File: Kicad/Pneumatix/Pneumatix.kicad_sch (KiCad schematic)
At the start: 16 parts, among them J1 705430004, J2 142-0701-801, J3 Conn_01x04_Socket, U1 E22-400T33S

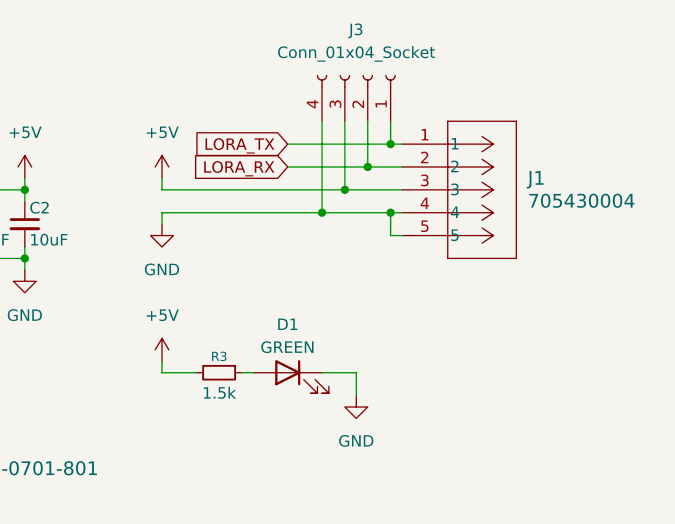
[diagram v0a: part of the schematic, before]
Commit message: wip: pcb and conception notes, fix: change molex 5 pins to 4 pins
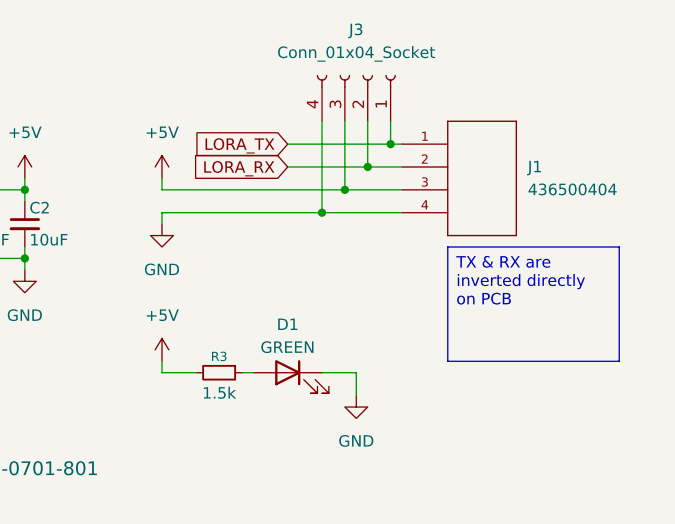
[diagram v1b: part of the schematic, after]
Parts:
- removed J1: 705430004, Pneumatix_Lib:CONN_SDA-70543-xxxx_05_MOL, symbol Pneumatix_Lib:705430004
- added J1: 436500404, Pneumatix_Lib:CONN_SD-43650-002_04_MOL, symbol Pneumatix_Lib:436500404
- H1, H2, H3: footprint MountingHole:MountingHole_2.2mm_M2 -> MountingHole:MountingHole_3.2mm_M3
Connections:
- net +5V: now also J1.3
- net GND: now also J1.4
- net LORA_RX: now also J1.2
- net LORA_TX: now also J1.1
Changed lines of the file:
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@@
 	(generator_version "10.0")
 	(paper "A4")
+	(text_box "TX & RX are inverted directly on PCB"
+		(exclude_from_sim no)
+		(at 213.36 85.09 0)
+		(size 19.05 12.7)
+		(margins 0.9525 0.9525 0.9525 0.9525)
+		(stroke
+			(width 0)
+			(type solid)
+		)
+		(fill
+			(type none)
+		)
+		(effects
+			(font
+				(size 1.27 1.27)
+			)
+			(justify left top)
+		)
+	)
 	(junction
 		(at 199.39 81.28)
@@
 	)
 	(junction
-		(at 207.01 81.28)
-		(diameter 0)
-		(color 0 0 0 0)
-	)
-	(junction
 		(at 204.47 76.2)
 		(diameter 0)
@@
 	(wire
 		(pts
-			(xy 208.28 83.82) (xy 207.01 83.82)
-		)
-		(stroke
-			(width 0)
-			(type default)
-		)
-	)
-	(wire
-		(pts
 			(xy 158.75 93.98) (xy 157.48 93.98)
 		)
@@
 	(wire
 		(pts
-			(xy 207.01 81.28) (xy 208.28 81.28)
+			(xy 181.61 81.28) (xy 208.28 81.28)
 		)
 		(stroke
@@
 	(wire
 		(pts
-			(xy 181.61 81.28) (xy 207.01 81.28)
-		)
-		(stroke
-			(width 0)
-			(type default)
-		)
-	)
-	(wire
-		(pts
 			(xy 181.61 82.55) (xy 181.61 81.28)
 		)
@@
 		(pts
 			(xy 181.61 78.74) (xy 181.61 77.47)
-		)
-		(stroke
-			(width 0)
-			(type default)
-		)
-	)
-	(wire
-		(pts
-			(xy 207.01 81.28) (xy 207.01 83.82)
 		)
 		(stroke
@@
 			)
 		)
-		(property "Footprint" "MountingHole:MountingHole_2.2mm_M2"
+		(property "Footprint" "MountingHole:MountingHole_3.2mm_M3"
 			(at 184.15 128.27 0)
 			(hide yes)
@@
 	)
 	(symbol
-		(lib_id "Pneumatix_Lib:705430004")
-		(at 208.28 73.66 0)
-		(unit 1)
-		(body_style 1)
-		(exclude_from_sim no)
-		(in_bom yes)
-		(on_board yes)
-		(in_pos_files yes)
-		(dnp no)
-		(fields_autoplaced yes)
-		(property "Reference" "J1"
-			(at 222.25 77.4699 0)
-			(show_name no)
-			(do_not_autoplace no)
-			(effects
-				(font
-					(size 1.524 1.524)
-				)
-				(justify left)
-			)
-		)
-		(property "Value" "705430004"
-			(at 222.25 80.0099 0)
-			(show_name no)
-			(do_not_autoplace no)
-			(effects
-				(font
-					(size 1.524 1.524)
-				)
-				(justify left)
-			)
-		)
-		(property "Footprint" "Pneumatix_Lib:CONN_SDA-70543-xxxx_05_MOL"
-			(at 208.28 73.66 0)
-			(hide yes)
-			(show_name no)
-			(do_not_autoplace no)
-			(effects
-				(font
-					(size 1.27 1.27)
-					(italic yes)
-				)
-			)
-		)
-		(property "Datasheet" "705430004"
-			(at 208.28 73.66 0)
-			(hide yes)
-			(show_name no)
-			(do_not_autoplace no)
-			(effects
-				(font
-					(size 1.27 1.27)
-					(italic yes)
-				)
-			)
-		)
-		(property "Description" ""
-			(at 208.28 73.66 0)
-			(hide yes)
-			(show_name no)
-			(do_not_autoplace no)
-			(effects
-				(font
-					(size 1.27 1.27)
-				)
-			)
-		)
-		(pin "2"
-		)
-		(pin "4"
-		)
-		(pin "1"
-		)
-		(pin "3"
-		)
-		(pin "5"
-		)
-		(instances
-			(project "Pneumatix"
-				(path "/f504cd5f-39a1-42fc-a563-dbfc0d20eebb"
-					(reference "J1")
-					(unit 1)
-				)
-			)
-		)
-	)
-	(symbol
 		(lib_id "Device:LED")
 		(at 195.58 99.06 0)
@@
 				(path "/f504cd5f-39a1-42fc-a563-dbfc0d20eebb"
 					(reference "C1")
+					(unit 1)
+				)
+			)
+		)
+	)
+	(symbol
+		(lib_id "Pneumatix_Lib:436500404")
+		(at 208.28 73.66 0)
+		(unit 1)
+		(body_style 1)
+		(exclude_from_sim no)
+		(in_bom yes)
+		(on_board yes)
+		(in_pos_files yes)
+		(dnp no)
+		(fields_autoplaced yes)
+		(property "Reference" "J1"
+			(at 222.25 76.1999 0)
+			(show_name no)
+			(do_not_autoplace no)
+			(effects
+				(font
+					(size 1.27 1.27)
+				)
+				(justify left)
+			)
+		)
+		(property "Value" "436500404"
+			(at 222.25 78.7399 0)
+			(show_name no)
+			(do_not_autoplace no)
+			(effects
+				(font
+					(size 1.27 1.27)
+				)
+				(justify left)
+			)
+		)
+		(property "Footprint" "Pneumatix_Lib:CONN_SD-43650-002_04_MOL"
+			(at 208.28 73.66 0)
+			(hide yes)
+			(show_name no)
+			(do_not_autoplace no)
+			(effects
+				(font
+					(size 1.27 1.27)
+				)
+				(justify bottom)
+			)
+		)
+		(property "Datasheet" "https://www.molex.com/en-us/products/part-detail-pdf/436500404?display=pdf"
+			(at 208.28 73.66 0)
+			(hide yes)
+			(show_name no)
+			(do_not_autoplace no)
+			(effects
+				(font
+					(size 1.27 1.27)
+				)
+				(justify bottom)
+			)
+		)
+		(property "Description" "Micro-Fit 3.0 Right-Angle Header, 3.00mm Pitch, Single Row, 4 Circuits, with PCB Press-fit Metal Retention Clip, 0.38Âµm Gold Plating, Glow-Wire Capable, Black"
+			(at 208.28 73.66 0)
+			(hide yes)
+			(show_name no)
+			(do_not_autoplace no)
+			(effects
+				(font
+					(size 1.27 1.27)
+				)
+				(justify bottom)
+			)
+		)
+		(property "MFR_NAME" "Molex"
+			(at 208.28 73.66 0)
+			(hide yes)
+			(show_name no)
+			(do_not_autoplace no)
+			(effects
+				(font
+					(size 1.27 1.27)
+				)
+				(justify bottom)
+			)
+		)
+		(property "MANUFACTURER_PART_NUMBER" "436500404"
+			(at 208.28 73.66 0)
+			(hide yes)
+			(show_name no)
+			(do_not_autoplace no)
+			(effects
+				(font
+					(size 1.27 1.27)
+				)
+				(justify bottom)
+			)
+		)
+		(pin "1"
+		)
+		(pin "3"
+		)
+		(pin "4"
+		)
+		(pin "2"
+		)
+		(instances
+			(project "Pneumatix"
+				(path "/f504cd5f-39a1-42fc-a563-dbfc0d20eebb"
+					(reference "J1")
 					(unit 1)
 				)
@@
 			)
 		)
-		(property "Footprint" "MountingHole:MountingHole_2.2mm_M2"
+		(property "Footprint" "MountingHole:MountingHole_3.2mm_M3"
 			(at 201.93 123.19 0)
 			(hide yes)
@@
 			)
 		)
-		(property "Footprint" "MountingHole:MountingHole_2.2mm_M2"
+		(property "Footprint" "MountingHole:MountingHole_3.2mm_M3"
 			(at 184.15 123.19 0)
 			(hide yes)

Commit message: wip: pcb components
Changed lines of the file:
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@@
 	(global_label "LORA_TX"
 		(shape input)
-		(at 128.27 81.28 180)
+		(at 128.27 81.28 0)
 		(fields_autoplaced yes)
 		(effects
@@
 				(size 1.27 1.27)
 			)
-			(justify right)
+			(justify left)
 		)
 		(property "Intersheetrefs" "${INTERSHEET_REFS}"
-			(at 117.4229 81.28 0)
+			(at 139.1171 81.28 0)
 			(hide yes)
 			(show_name no)
@@
 					(size 1.27 1.27)
 				)
-				(justify right)
+				(justify left)
 			)
 		)

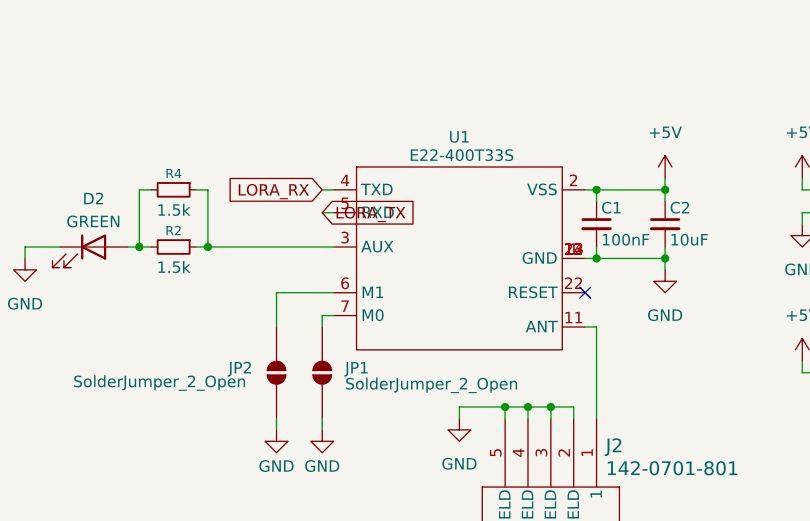
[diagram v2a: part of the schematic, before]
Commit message: wip: add thermal pads and plane for heat dissipation
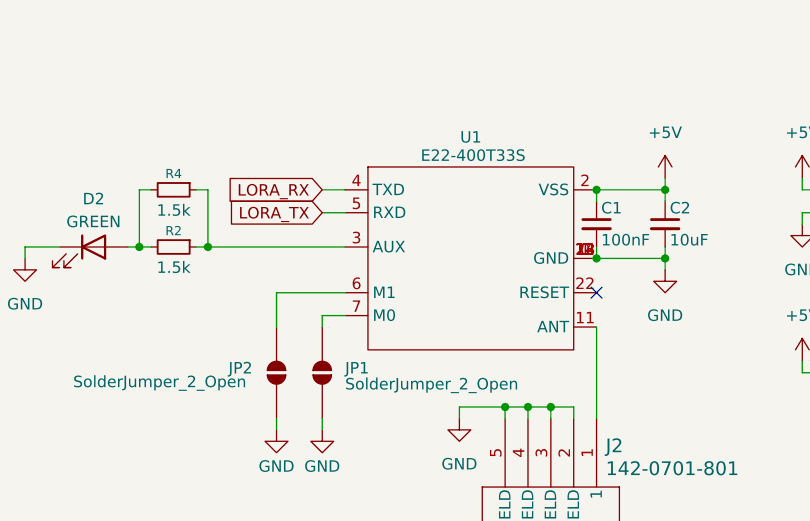
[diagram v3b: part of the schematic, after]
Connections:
- net GND: now also U1.0 (GND)

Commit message: wip: add pu/pd for M0 and M1, remake traces and swap gnd/signal/passive components plane
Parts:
- removed J3: Conn_01x04_Socket, Connector_PinSocket_2.54mm:PinSocket_1x04_P2.54mm_Vertical, symbol Connector:Conn_01x04_Socket
- added J3: Conn_01x06_Socket, Connector_PinHeader_2.54mm:PinHeader_1x06_P2.54mm_Vertical, symbol Connector:Conn_01x06_Socket
- added R5, R6, R7, R8: 1.5k, Resistor_SMD:R_0603_1608Metric, symbol Device:R_Small
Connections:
- net +5V: now also JP1.2 (B), JP2.2 (B), J3.5 (Pin_5)
- net GND: now also J3.6 (Pin_6), R6.2, R8.2; no longer JP1.2 (B), JP2.2 (B)
- net LORA_RX: now also J3.4 (Pin_4)
- net LORA_TX: now also J3.3 (Pin_3)
- net at JP1.1 (A): now also R5.2; no longer U1.7 (M0)
- net at JP2.1 (A): now also R7.2; no longer U1.6 (M1)
- new net LORA_M0: J3.2 (Pin_2), R7.1, R8.1, U1.7 (M0)
- new net LORA_M1: J3.1 (Pin_1), R5.1, R6.1, U1.6 (M1)
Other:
- moved on the sheet: C1, C2, D1, JP1, R3

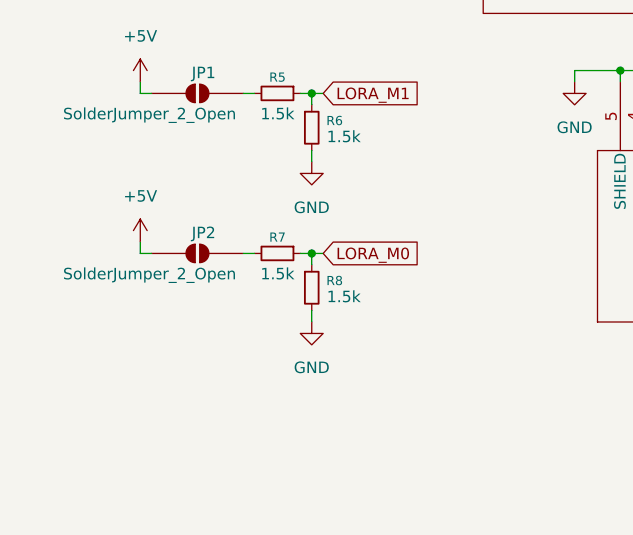
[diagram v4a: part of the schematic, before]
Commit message: wip: fix voltage divider for m0 and m1, reduce 2.54 debug header to 2.00mm
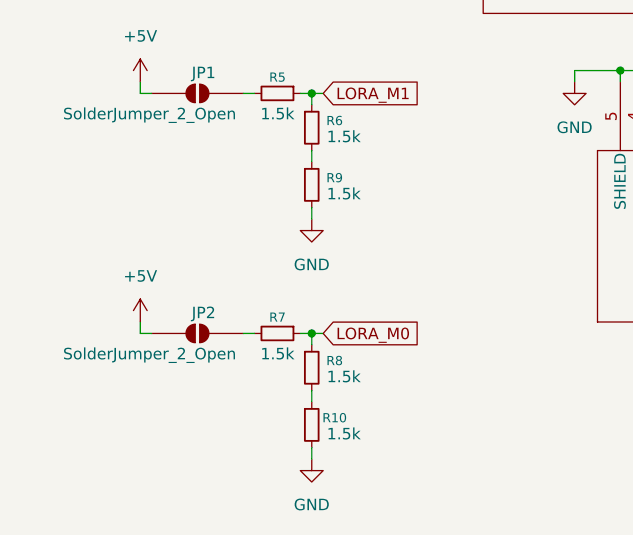
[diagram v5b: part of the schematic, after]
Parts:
- added R10, R9: 1.5k, Resistor_SMD:R_0603_1608Metric, symbol Device:R_Small
- J3: footprint Connector_PinHeader_2.54mm:PinHeader_1x06_P2.54mm_Vertical -> Connector_PinHeader_2.00mm:PinHeader_1x06_P2.00mm_Vertical
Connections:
- net GND: now also R10.2, R9.2; no longer R6.2, R8.2
- new net: R10.1, R8.2
- new net: R6.2, R9.1
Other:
- moved on the sheet: JP2, R7, R8

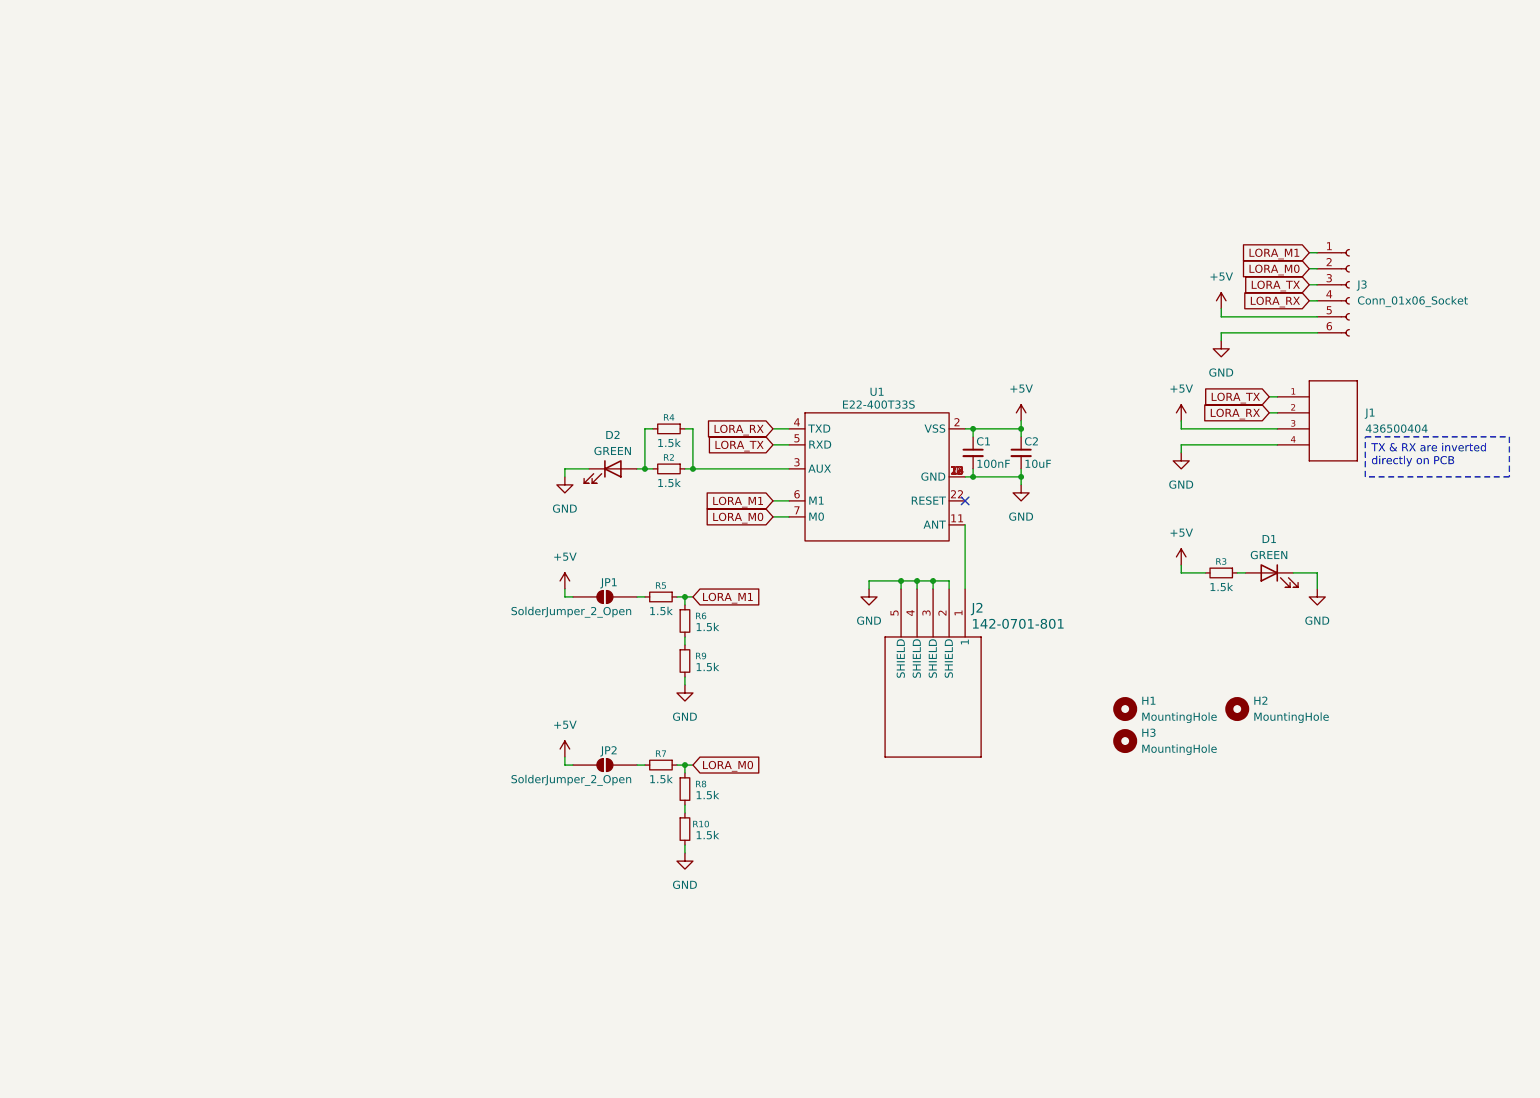
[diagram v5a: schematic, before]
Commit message: wip: silkscreen and adjustements
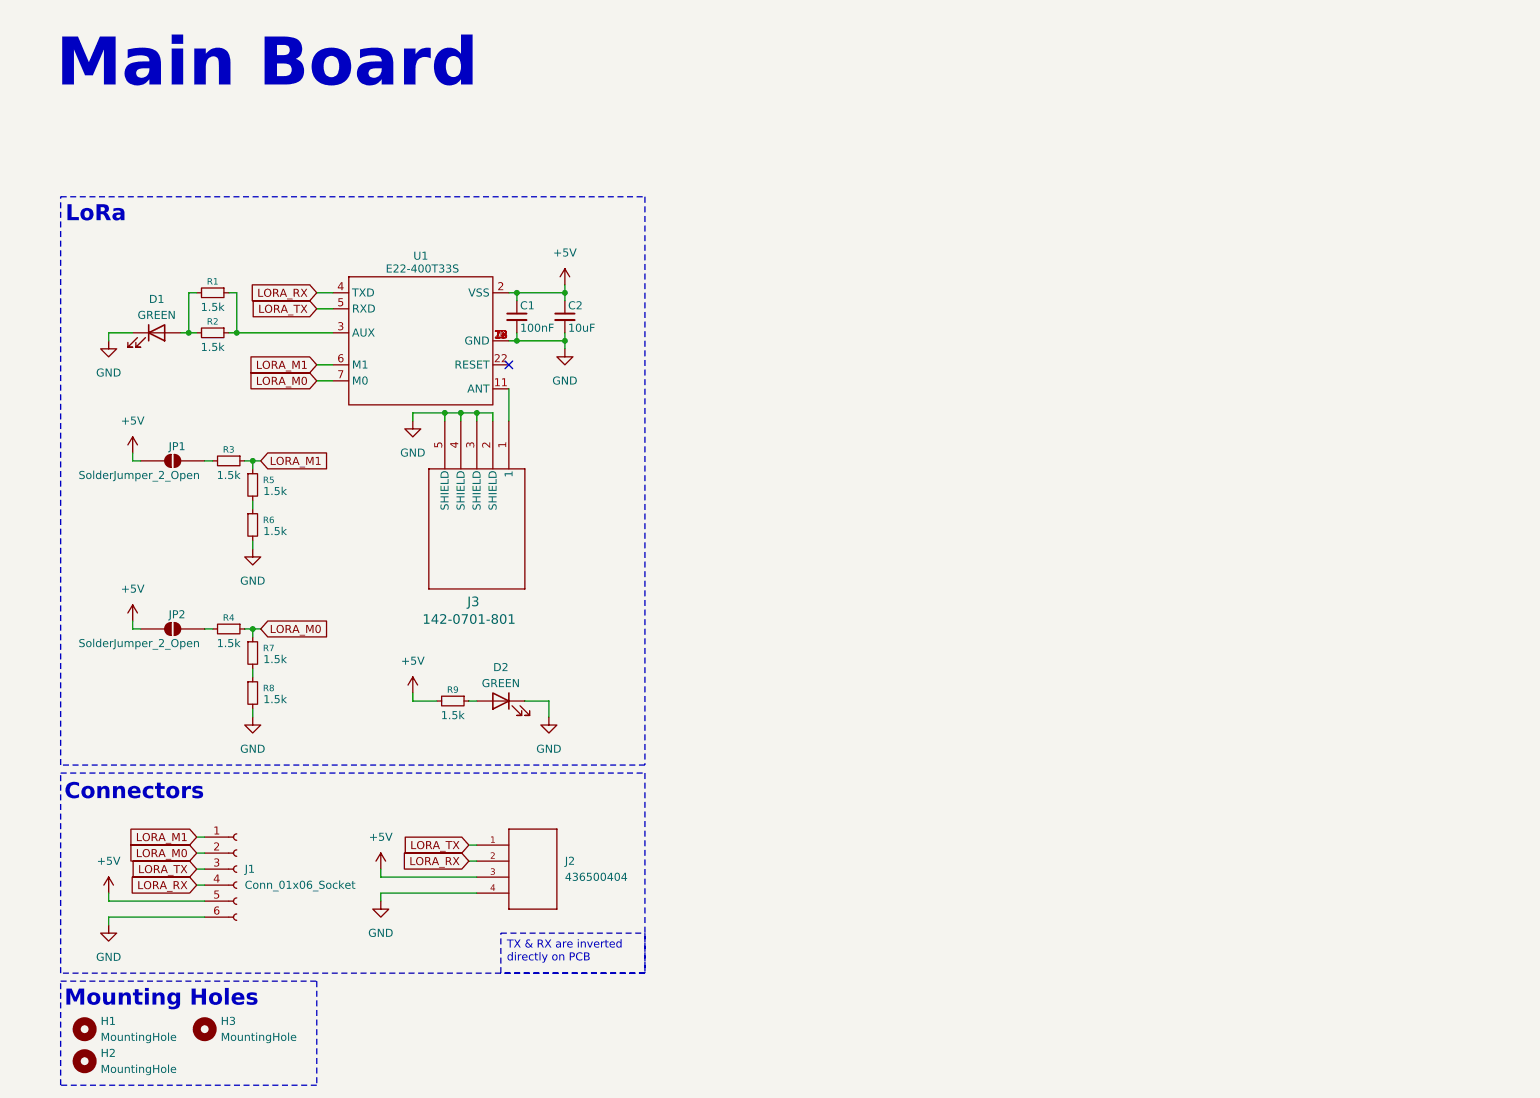
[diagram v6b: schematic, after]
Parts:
- renumbered D2 to D1, D1 to D2, H3 to H2, H2 to H3, J3 to J1, J1 to J2, J2 to J3, R4 to R1, R5 to R3, R7 to R4, R6 to R5, R9 to R6, R8 to R7, R10 to R8, R3 to R9
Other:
- note added: "Connectors"
- note added: "LoRa"
- note added: "Main Board"
- note added: "Mounting Holes"
- moved on the sheet: C1, C2, D1, D2, H1, H2, H3, J1, J2, J3, JP1, JP2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

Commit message: wip: pcb adjustements
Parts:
- removed R1: 1.5k, Resistor_SMD:R_0603_1608Metric, symbol Device:R_Small
- added C3: 100uF, Capacitor_SMD:C_0603_1608Metric, symbol Device:C_Small
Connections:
- net +5V: now also C3.1
- net GND: now also C3.2
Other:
- moved on the sheet: C1, C2, D1, J3, R2, U1
